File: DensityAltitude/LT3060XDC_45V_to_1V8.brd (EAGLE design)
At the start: 63.5 x 57.1 mm, 15 parts, among them U1 V_REG_LD1086V

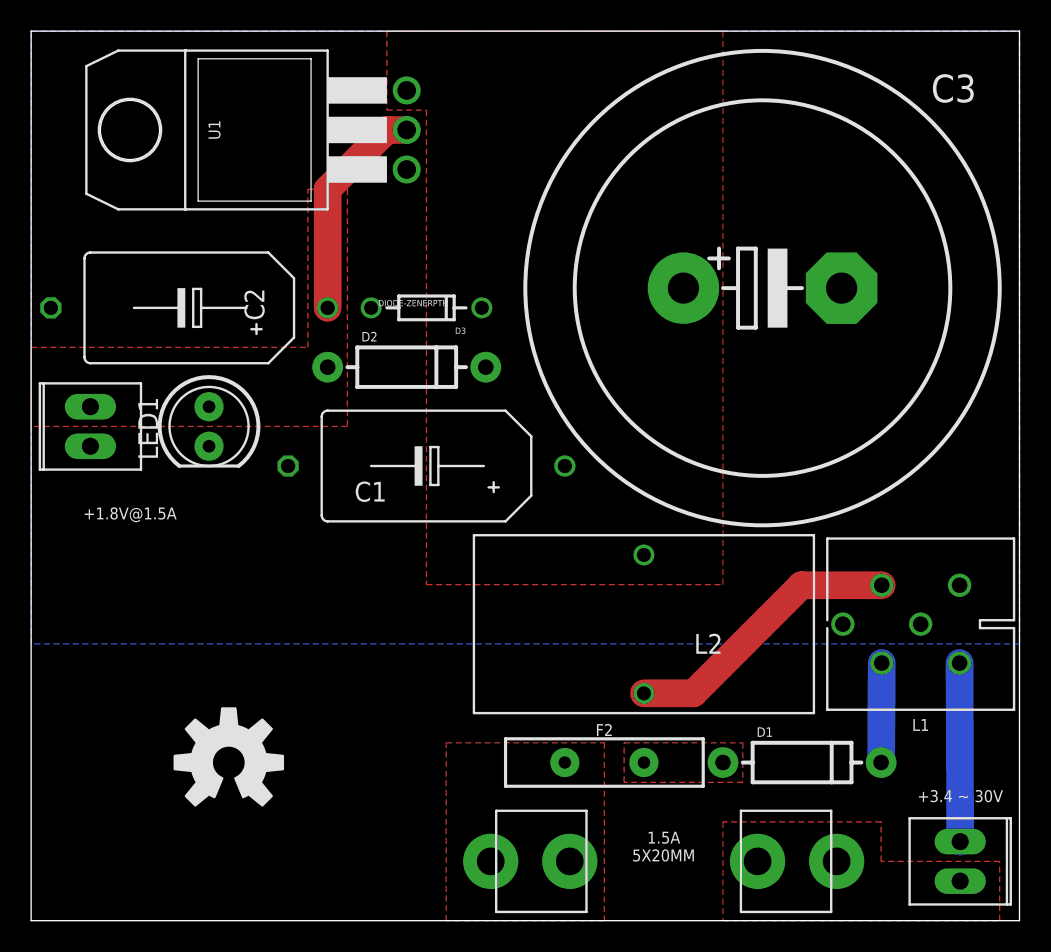
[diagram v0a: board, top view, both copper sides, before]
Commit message: Moved 1V8 voltage regulators from DensityAltitude.lbr to 1V8.lbr More layout work for various high input voltage regulators A bit more work on LowduinoPTH_v2
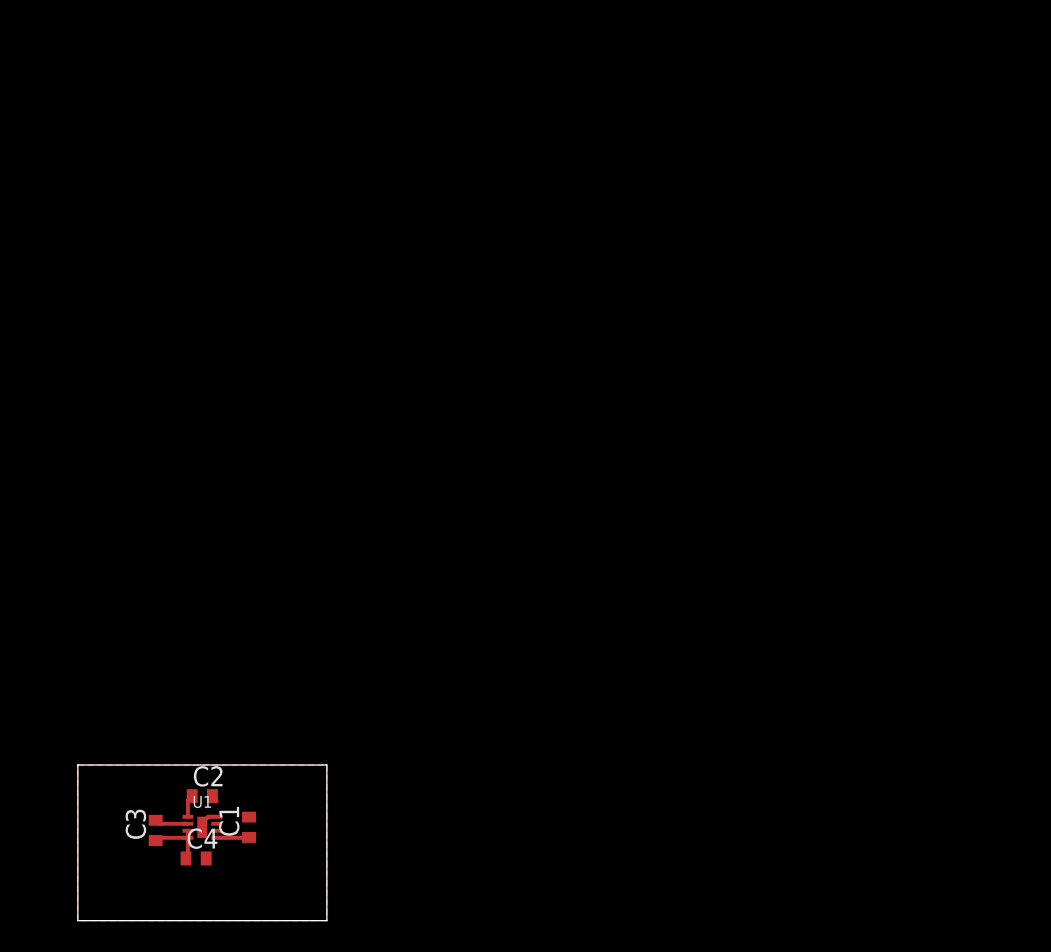
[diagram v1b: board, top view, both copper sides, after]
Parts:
- removed D1, D2: (no value), SparkFun-DiscreteSemi:DIODE-1N4001
- removed D3: DIODE-ZENERPTH, SparkFun-DiscreteSemi:DIODE-ZENER
- removed F1: FUSE5X20MM, DensityAltitude:FUSE_1A3399
- removed F2: PTCPTH, DensityAltitude:PTC
- removed JP1, JP2: (no value), DensityAltitude:1X02_282834-2
- removed L1: BNX002, 1V8:BNX002
- removed L2: 2121-RC-VERT, DensityAltitude:2121-RC-VERT
- removed LED1: (no value), SparkFun-LED:LED5MM
- removed U$2: (no value), SparkFun-Aesthetics:OSHW-LOGO-L
- added C4: 10uF, rcl:C0402
- C1: value 10uF -> 1uF; device 1V8:KEMET_E -> rcl:C0402
- C2: value 10uF -> 10nF; device 1V8:KEMET_E -> rcl:C0402
- C3: value (none) -> 10nF; device rcl:EB30D -> rcl:C0402
- U1: value V_REG_LD1086V -> LT3060EDC; device DensityAltitude:TO-220-SINGLE -> 1V8:LINEAR_DC8
- moved C3 52.3 mm to (8.00, 5.80), turned to 90 degrees
- moved U1 45.0 mm to (11.0, 6.00), turned to 0 degrees
- moved C2 31.4 mm to (11.0, 8.00), turned to 0 degrees
- moved C1 25.9 mm to (14.0, 6.00), turned to 90 degrees
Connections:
- removed net DIODE1: D1.C, L1.B
- removed net FILTERED: C1.+, C3.+, D2.C, D3.P$1, L2.2, U1.IN
- removed net FUSE1: F1.3, F1.4, F2.P$1
- removed net FUSE2: D1.A, F2.P$2
- removed net GND-ISO: C1.-, C2.-, C3.-, D3.P$2, JP2.P$1, L1.CG, L1.CG1, L1.CG2, LED1.K, U1.GND
- removed net N$1: L1.CB, L2.1
- removed net VCC: C2.+, D2.A, JP2.P$2, LED1.A, U1.OUT
- new net N$4: C3.2, U1.2
- new net N$6: C2.1, U1.1
- new net OUT: C3.1, C4.1, U1.3, U1.4
- net GND: now also C1.2, C2.2, C4.2, U1.8, U1.9; no longer JP1.P$1, L1.PSG
- net VIN: now also C1.1, U1.5, U1.6, U1.7; no longer F1.1, F1.2, JP1.P$2
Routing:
- net N$1: track 18.2 -> 0.00 mm
- net VCC: track 14.3 -> 0.00 mm
- net GND: track 11.5 -> 1.77 mm
- net DIODE1: track 6.39 -> 0.00 mm
- net OUT: track 0.00 -> 3.97 mm
- net N$4: track 0.00 -> 2.17 mm
- net VIN: track 0.00 -> 2.09 mm
- net N$6: track 0.00 -> 1.44 mm
- added copper zone on layer 1, net GND
- removed copper zone on layer 1, net FILTERED
- removed copper zone on layer 1, net FUSE1
- removed copper zone on layer 1, net FUSE2
- removed copper zone on layer 16, net GND-ISO
- removed copper zone on layer 1, net VCC
- removed copper zone on layer 1, net VIN
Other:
- board size 63.5 x 57.1 mm -> 16 x 10 mm
- board text removed: "+1.8V@1.5A"
- board text removed: "+3.4 ~ 30V"
- board text removed: "1.5A 5X20MM"
